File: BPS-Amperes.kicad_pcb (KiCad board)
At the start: 2 copper layers, 40 x 50 mm, 37 parts, among them J1 Conn_02x10_Odd_Even, J2 ShuntConn, U1 INA186A3IDDFT, U2 OPA2196, U3 LTC2315, U4 REF1930AIDDCT

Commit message: Initial Grouped Layout
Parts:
- C3, D2, LOGO0, LOGO1, R6, R7, TP2, TP3, U1, U2: moved to B.Cu
- moved C12 79.9 mm to (146.9, 103.6), turned to 90 degrees
- moved D2 79.9 mm to (166.6, 82.4), turned to 90 degrees
- moved C11 77.6 mm to (150.5, 103.6), turned to 90 degrees
- moved R6 77.2 mm to (168.8, 82.4), turned to 90 degrees
- moved LOGO1 75.6 mm to (161.0, 107.8), turned to 180 degrees
- moved C13 73.4 mm to (135.5, 94.8), turned to -90 degrees
- moved C9 56.2 mm to (164.5, 106.8)
- moved TP3 55.1 mm to (160.4, 110.8), turned to 180 degrees
- moved C10 53.1 mm to (164.4, 103.1)
- moved TP2 43.5 mm to (164.4, 110.8), turned to 180 degrees
- moved FB2 41.9 mm to (153.4, 103.7), turned to -90 degrees
- moved FB1 39.7 mm to (156.6, 103.7), turned to -90 degrees
- moved U4 38.9 mm to (155.1, 99.3), turned to 180 degrees
- moved TP1 34.2 mm to (135.2, 110.8)
- moved LOGO0 24.7 mm to (139.3, 73.6), turned to 180 degrees
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
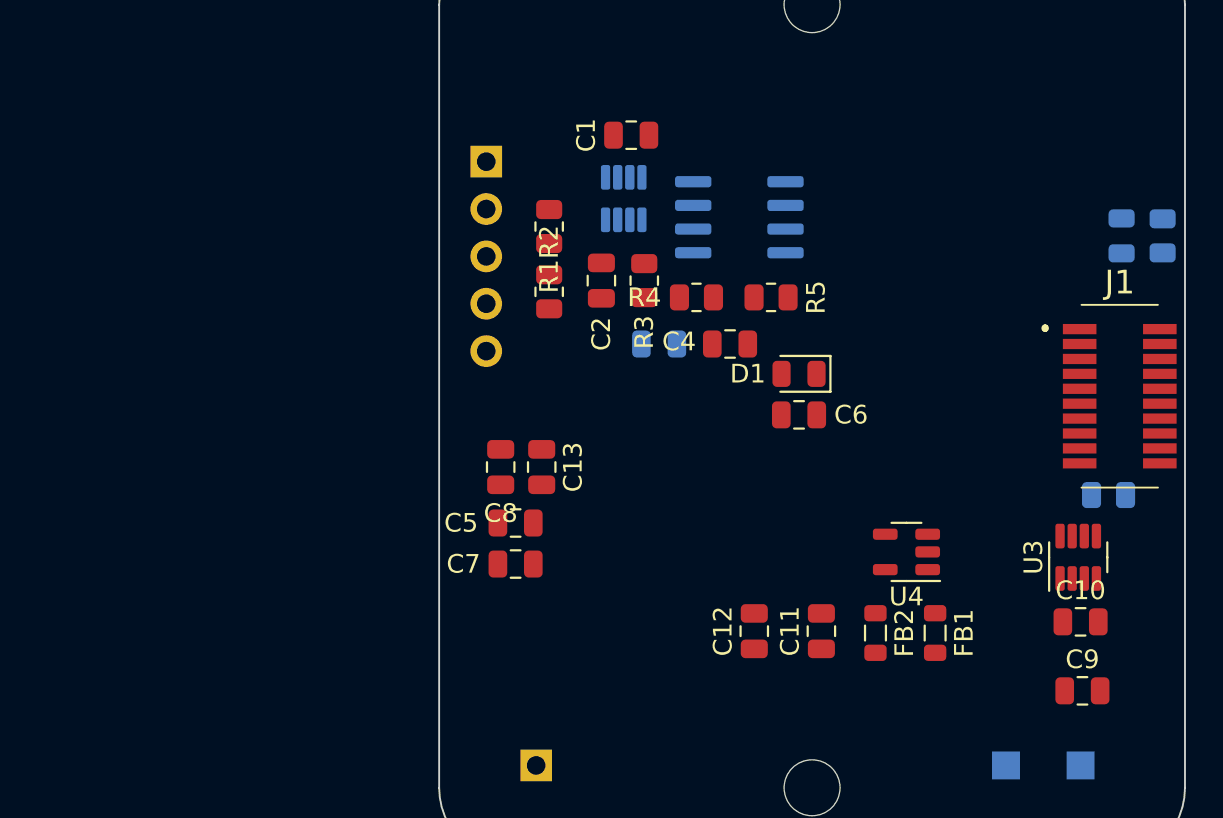
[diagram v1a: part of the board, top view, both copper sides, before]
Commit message: Moved components to back of PCB, currently rearranging
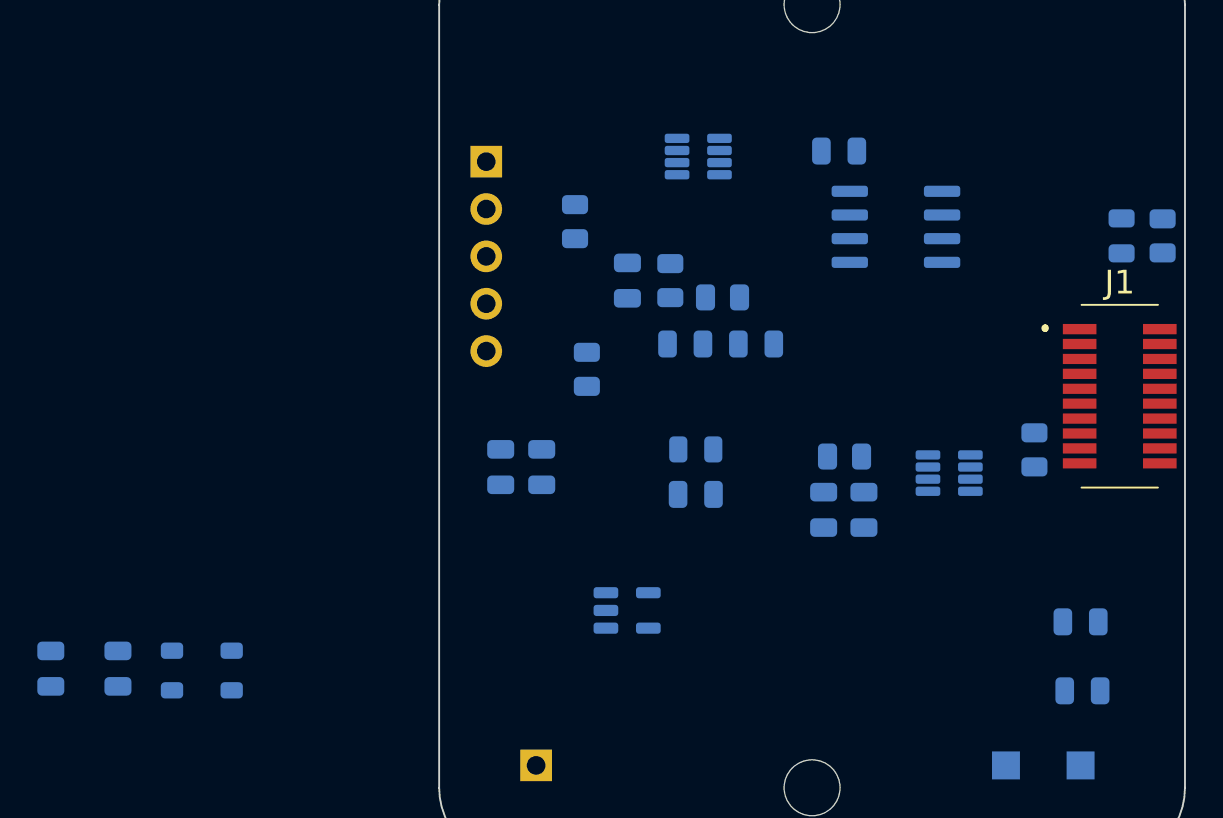
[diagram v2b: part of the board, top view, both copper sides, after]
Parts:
- C1, C10, C11, C12, C13, C2, C4, C5, C6, C7, C8, C9, D1, FB1, FB2, R1, R2, R3, R4, R5, U3, U4: moved to B.Cu
- moved LOGO1 46.9 mm to (118.9, 87.2)
- moved C12 37.8 mm to (109.2, 105.6)
- moved FB2 37.8 mm to (115.7, 105.7)
- moved C11 37.8 mm to (112.8, 105.6)
- moved FB1 37.8 mm to (118.9, 105.7)
- moved LOGO0 20.0 mm to (119.4, 74.7)
- moved C7 18.9 mm to (152.8, 97.1), turned to 90 degrees
- moved C5 16.5 mm to (150.6, 97.1), turned to 90 degrees
- moved U4 15.3 mm to (140.1, 102.5), turned to 0 degrees
- moved C1 11.2 mm to (151.4, 77.9)
- moved R5 9.40 mm to (151.7, 94.2), turned to 180 degrees
- moved U2 8.41 mm to (154.5, 81.9)
- moved U3 8.26 mm to (157.4, 95.1), turned to 0 degrees
- moved C6 6.99 mm to (143.8, 96.3), turned to 0 degrees
- moved D1 6.86 mm to (143.8, 93.9), turned to 0 degrees
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
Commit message: Layout updates
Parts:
- added J3: PassthroughConn, Connector_PinSocket_2.54mm:PinSocket_1x05_P2.54mm_Vertical, B.Cu at (124.7, 99.6)
- added J4: TestConn, Connector_PinSocket_2.54mm:PinSocket_1x05_P2.54mm_Horizontal, B.Cu at (195.8, 71.0)
- added MH3: M.3, MountingHole:MountingHole_2.7mm_M2.5, F.Cu at (154.6, 104.6)
- added MH4: M.3, MountingHole:MountingHole_2.7mm_M2.5, F.Cu at (125.7, 80.6)
- moved TP2 79.6 mm to (101.5, 62.0)
- moved TP3 79.6 mm to (97.5, 62.0)
- moved C10 78.3 mm to (86.3, 108.9)
- moved C9 78.3 mm to (86.4, 112.6)
- moved R6 64.5 mm to (104.4, 85.2)
- moved D2 64.5 mm to (102.2, 85.2)
- moved R7 64.0 mm to (98.0, 97.8)
- moved C2 63.9 mm to (76.3, 81.0)
- moved C4 63.9 mm to (83.2, 84.4)
- moved C5 63.9 mm to (86.8, 93.3)
- moved C6 63.9 mm to (80.0, 92.5)
- moved C7 63.9 mm to (89.0, 93.3)
- moved C8 63.9 mm to (69.5, 91.0)
- moved D1 63.9 mm to (80.0, 90.0)
- moved R1 63.9 mm to (73.5, 77.8)
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
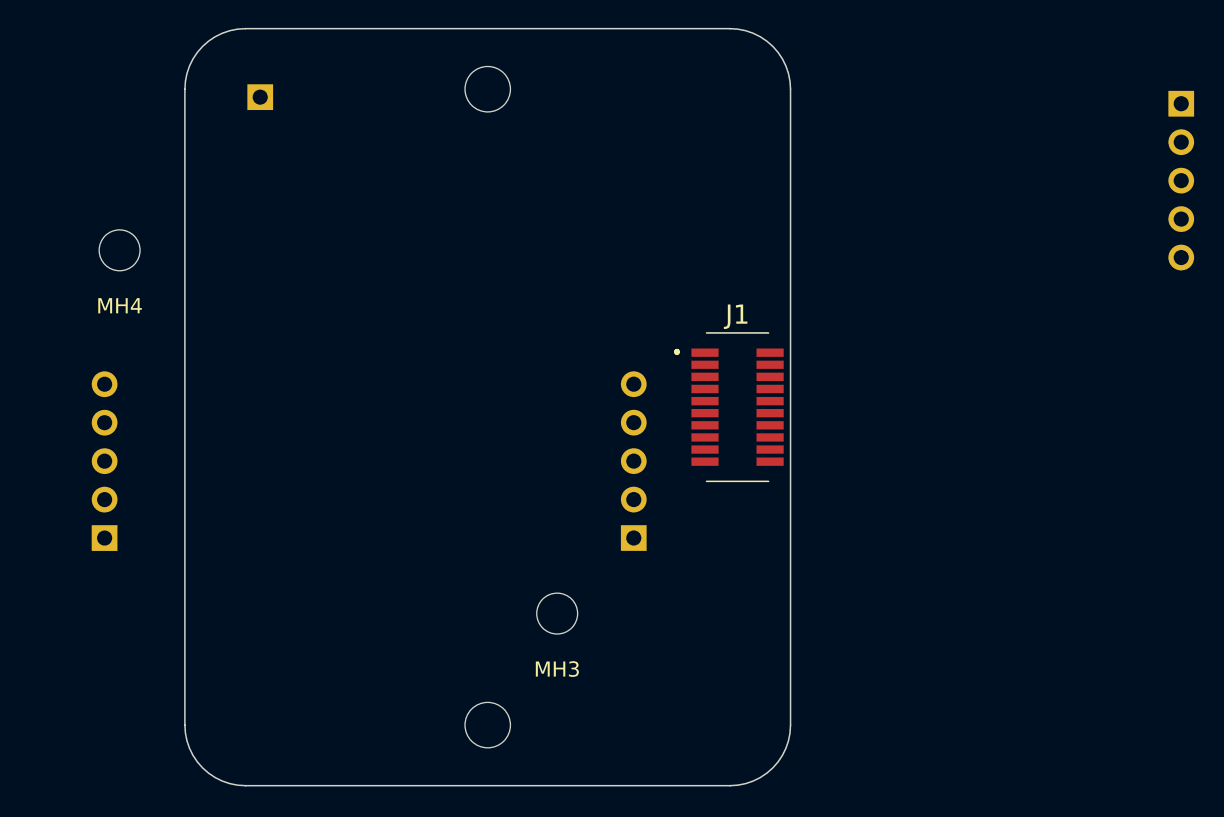
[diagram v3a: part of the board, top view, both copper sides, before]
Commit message: Possible Main components orientation
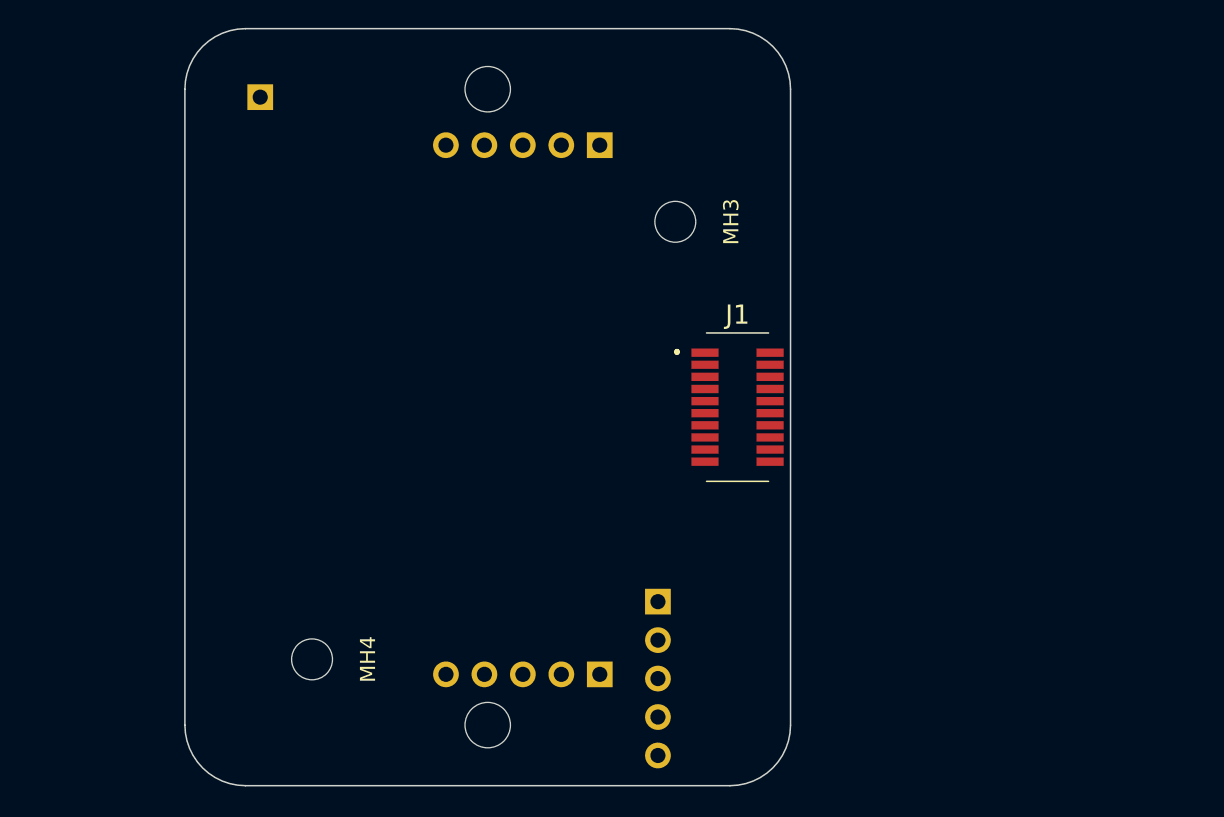
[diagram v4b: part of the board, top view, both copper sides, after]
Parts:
- moved J4 47.7 mm to (161.2, 103.8)
- moved J3 33.9 mm to (157.4, 108.6), turned to 90 degrees
- moved MH4 29.9 mm to (138.4, 107.7), turned to -90 degrees
- moved MH3 27.0 mm to (162.4, 78.8), turned to -90 degrees
- moved J2 26.0 mm to (157.4, 73.7), turned to 90 degrees

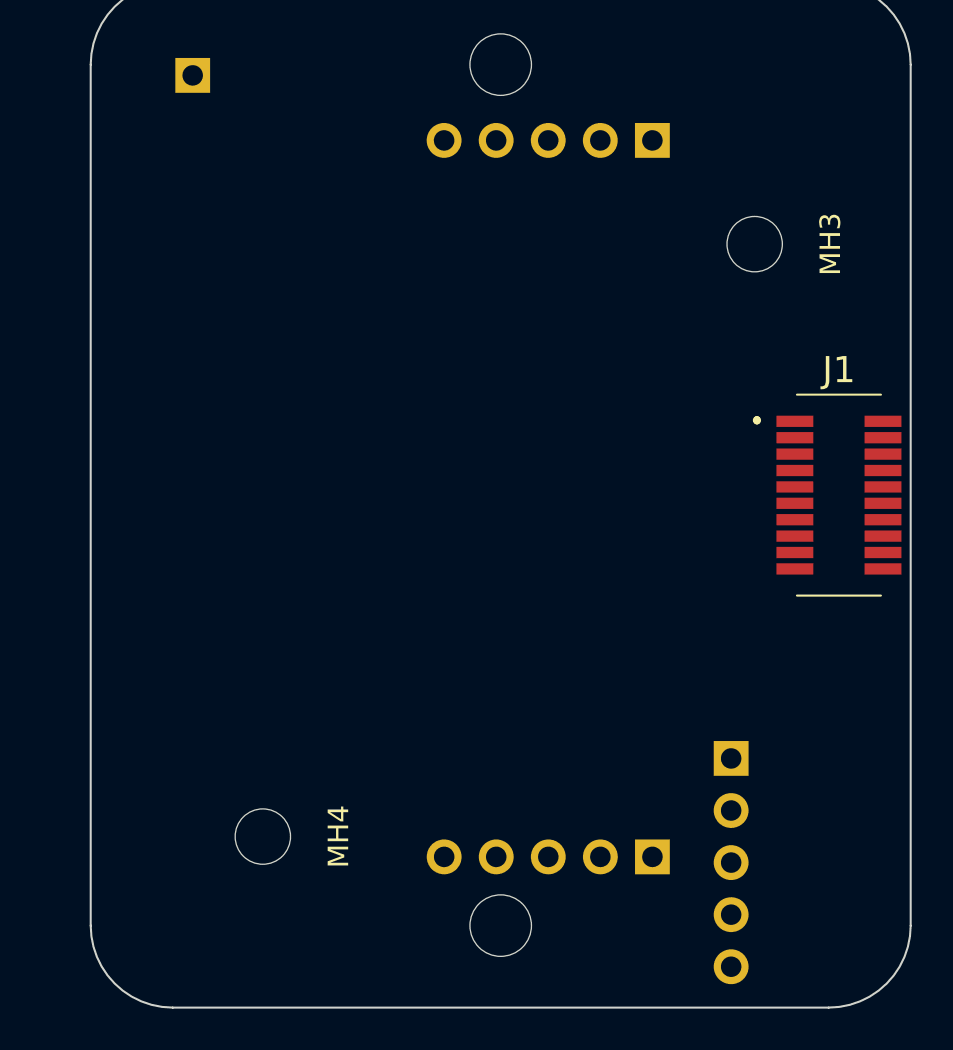
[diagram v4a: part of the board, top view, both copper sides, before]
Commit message: Sike we don't need mounting holes
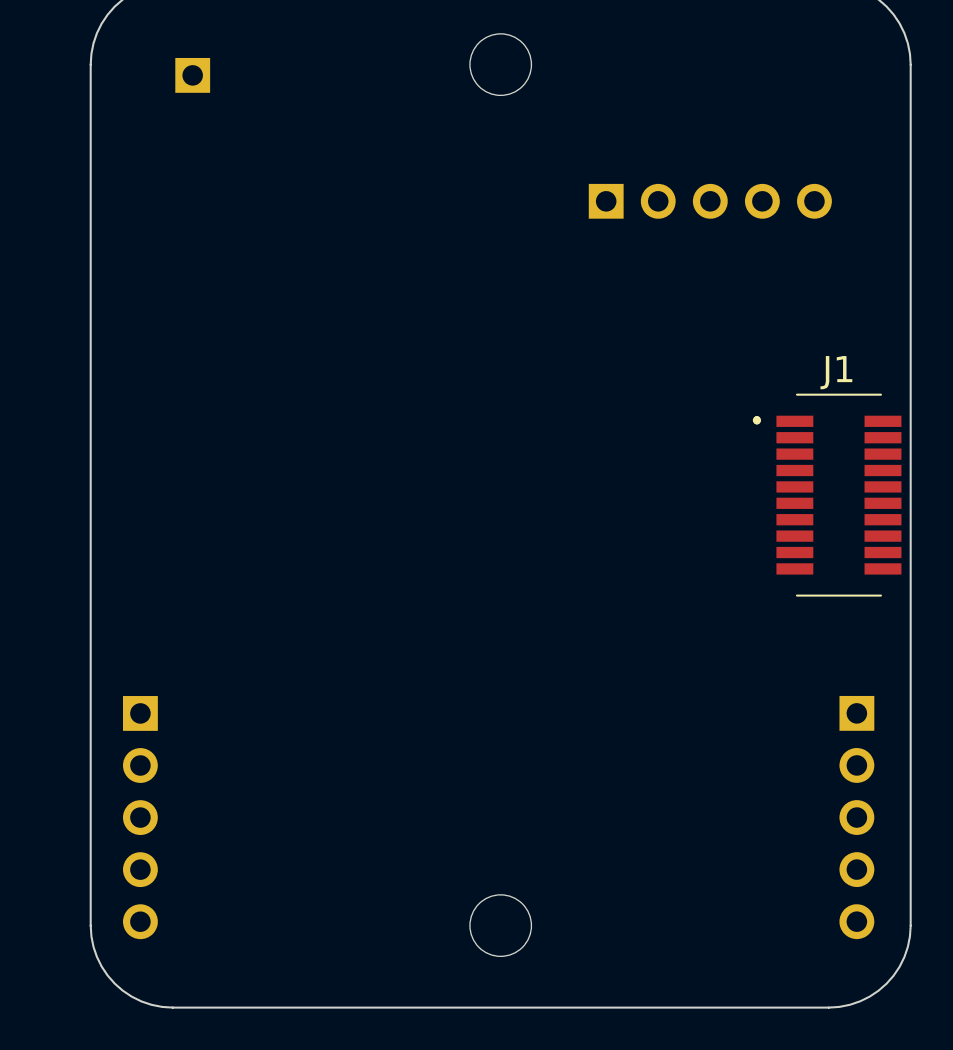
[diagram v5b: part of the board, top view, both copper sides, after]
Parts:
- removed MH3, MH4: M.3, MountingHole:MountingHole_2.7mm_M2.5
- moved J2 37.5 mm to (132.4, 101.7), turned to 180 degrees
- moved J4 27.9 mm to (155.1, 76.7), turned to -90 degrees
- moved J3 12.2 mm to (167.4, 101.6), turned to 180 degrees
